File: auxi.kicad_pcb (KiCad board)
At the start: 2 copper layers, 0 parts

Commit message: feat(pcb): Add design settings, update schematic notes, and modify MP1584 module footprint
- Introduced comprehensive design settings in `auxi.kicad_pro` for improved PCB layout control, including defaults for various design elements and DRC rules.
- Updated schematic notes in `auxi.kicad_sch` to reflect changes in battery connector specifications and additional circuit details.
- Enhanced the MP1584 module footprint in `MP1584_Mini_PROVISIONAL.kicad_mod` with corrected dimensions, improved pad layout, and updated silk screen labels for clarity.
- Added a new PCB placement image `auxi_pcb_placement.png` to the documentation for better assembly guidance.
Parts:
- added C1: 470uF 25V, Capacitor_THT:CP_Radial_D10.0mm_P5.00mm, F.Cu at (159.0, 112.0)
- added C10: 100nF 50V X7R, Capacitor_SMD:C_1206_3216Metric, F.Cu at (157.5, 190.5)
- added C11: 470uF 25V, Capacitor_THT:CP_Radial_D10.0mm_P5.00mm, F.Cu at (122.5, 164.0)
- added C12: 10uF 25V X7R, Capacitor_SMD:C_1206_3216Metric, F.Cu at (136.0, 151.0)
- added C13: 100nF 50V X7R, Capacitor_SMD:C_1206_3216Metric, F.Cu at (141.2, 151.0)
- added C14: 10uF 25V X7R, Capacitor_SMD:C_1206_3216Metric, F.Cu at (127.5, 109.5)
- added C15: 100nF 50V X7R, Capacitor_SMD:C_1206_3216Metric, F.Cu at (132.5, 109.5)
- added C16: 10uF 25V X7R, Capacitor_SMD:C_1206_3216Metric, F.Cu at (110.5, 162.0)
- added C17: 100nF 50V X7R, Capacitor_SMD:C_1206_3216Metric, F.Cu at (110.5, 166.0)
- added C18: 10uF 25V X7R, Capacitor_SMD:C_1206_3216Metric, F.Cu at (126.5, 195.0)
- added C19: 100nF 50V X7R, Capacitor_SMD:C_1206_3216Metric, F.Cu at (129.0, 195.0)
- added C2: 100nF 50V X7R, Capacitor_SMD:C_1206_3216Metric, F.Cu at (170.0, 115.0)
- added C20: 10uF 25V X7R, Capacitor_SMD:C_1206_3216Metric, F.Cu at (111.0, 113.0)
- added C21: 100nF 50V X7R, Capacitor_SMD:C_1206_3216Metric, F.Cu at (111.0, 117.0)
- added C3: 220uF 25V, Capacitor_THT:CP_Radial_D8.0mm_P3.50mm, F.Cu at (138.8, 117.5)
- added C4: 100nF 50V X7R, Capacitor_SMD:C_1206_3216Metric, F.Cu at (139.0, 106.5)
- added C5: 22uF 25V, Capacitor_THT:CP_Radial_D5.0mm_P2.00mm, F.Cu at (111.5, 183.0)
- added C6: 100nF 50V X7R, Capacitor_SMD:C_1206_3216Metric, F.Cu at (112.5, 188.0)
- added C7: 100uF 16V, Capacitor_THT:CP_Radial_D6.3mm_P2.50mm, F.Cu at (140.2, 166.0)
- added C8: 10uF 25V X7R, Capacitor_SMD:C_1206_3216Metric, F.Cu at (143.0, 184.0)
- added C9: 100uF 16V, Capacitor_THT:CP_Radial_D6.3mm_P2.50mm, F.Cu at (182.8, 185.0)
- added D1: 1N5819, Diode_THT:D_DO-41_SOD81_P10.16mm_Horizontal, F.Cu at (150.5, 190.0)
- added H1: MountingHole_3.2mm_M3, MountingHole:MountingHole_3.2mm_M3, F.Cu at (105.0, 105.0)
- added H2: MountingHole_3.2mm_M3, MountingHole:MountingHole_3.2mm_M3, F.Cu at (185.0, 105.0)
- added H3: MountingHole_3.2mm_M3, MountingHole:MountingHole_3.2mm_M3, F.Cu at (105.0, 195.0)
- added H4: MountingHole_3.2mm_M3, MountingHole:MountingHole_3.2mm_M3, F.Cu at (185.0, 195.0)
- added J_BAT1: XT30 BAT 2S, Connector_AMASS:AMASS_XT30UPB-M_1x02_P5.0mm_Vertical, F.Cu at (185.5, 120.0)
- added J_LED_FRONT1: LED_FRONT (ROJO), Connector_PinHeader_2.54mm:PinHeader_1x02_P2.54mm_Vertical, F.Cu at (102.5, 176.0)
- added J_LED_LEFT1: LED_LEFT (AMARILLO), Connector_PinHeader_2.54mm:PinHeader_1x02_P2.54mm_Vertical, F.Cu at (132.5, 197.5)
- added J_LED_POWER1: POWER LED (azul), Connector_PinHeader_2.54mm:PinHeader_1x02_P2.54mm_Vertical, F.Cu at (187.5, 128.0)
- added J_LED_RIGHT1: LED_RIGHT (VERDE), Connector_PinHeader_2.54mm:PinHeader_1x02_P2.54mm_Vertical, F.Cu at (110.5, 103.0)
- added J_MOTOR_LEFT1: MOTOR_LEFT, TerminalBlock_Phoenix:TerminalBlock_Phoenix_MKDS-1,5-2-5.08_1x02_P5.08mm_Horizontal, F.Cu at (140.5, 194.5)
- added J_MOTOR_RIGHT1: MOTOR_RIGHT, TerminalBlock_Phoenix:TerminalBlock_Phoenix_MKDS-1,5-2-5.08_1x02_P5.08mm_Horizontal, F.Cu at (151.0, 107.0)
- added J_SENSOR_FRONT1: SENSOR_FRONT (VL53L0X), Connector_JST:JST_XH_B5B-XH-A_1x05_P2.50mm_Vertical, F.Cu at (104.5, 161.0)
- added J_SENSOR_LEFT1: SENSOR_LEFT (VL53L0X), Connector_JST:JST_XH_B5B-XH-A_1x05_P2.50mm_Vertical, F.Cu at (122.0, 196.5)
- added J_SENSOR_RIGHT1: SENSOR_RIGHT (VL53L0X), Connector_JST:JST_XH_B5B-XH-A_1x05_P2.50mm_Vertical, F.Cu at (104.5, 112.0)
- added J_SWITCH1: SWITCH ON-OFF, TerminalBlock_Phoenix:TerminalBlock_Phoenix_MKDS-1,5-2-5.08_1x02_P5.08mm_Horizontal, F.Cu at (175.0, 106.0)
- added R1: 1.5k, Resistor_SMD:R_1206_3216Metric, F.Cu at (183.0, 129.3)
- added R2: 10k, Resistor_SMD:R_1206_3216Metric, F.Cu at (127.5, 118.5)
- added R3: 4.7k DNP, Resistor_SMD:R_1206_3216Metric, F.Cu at (160.0, 167.6)
- added R4: 4.7k DNP, Resistor_SMD:R_1206_3216Metric, F.Cu at (160.0, 175.2)
- added R5: 470, Resistor_SMD:R_1206_3216Metric, F.Cu at (108.0, 177.0)
- added R6: 470, Resistor_SMD:R_1206_3216Metric, F.Cu at (135.0, 192.5)
- added R7: 470, Resistor_SMD:R_1206_3216Metric, F.Cu at (111.5, 108.3)
- added U_CAM1: ESP32-CAM AI Thinker (fila 5V), Connector_PinSocket_2.54mm:PinSocket_1x08_P2.54mm_Vertical, F.Cu at (142.5, 154.9)
- added U_CAM2: ESP32-CAM AI Thinker (fila 3V3), Connector_PinSocket_2.54mm:PinSocket_1x08_P2.54mm_Vertical, F.Cu at (142.5, 132.1)
- added U_ESP_J1: ESP32-S3-DevKitC-1 N16R8 (J1), Connector_PinSocket_2.54mm:PinSocket_1x22_P2.54mm_Vertical, F.Cu at (154.0, 139.7)
- added U_ESP_J3: ESP32-S3-DevKitC-1 N16R8 (J3), Connector_PinSocket_2.54mm:PinSocket_1x22_P2.54mm_Vertical, F.Cu at (176.9, 139.7)
- added U_MP1584: MP1584EN mini (5.0V), auxi:MP1584_Mini_PROVISIONAL, F.Cu at (129.2, 179.5)
- added U_TB1: TB6612FNG breakout (logica), Connector_PinSocket_2.54mm:PinSocket_1x08_P2.54mm_Vertical, F.Cu at (134.9, 122.9)
- added U_TB2: TB6612FNG breakout (potencia), Connector_PinSocket_2.54mm:PinSocket_1x08_P2.54mm_Vertical, F.Cu at (134.9, 105.1)
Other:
- board outline added: 90 x 100 mm
- board text added: "5V"
- board text added: "ANT/FPC"
- board text added: "ANTENNA - NO COPPER"
- board text added: "ESP32-CAM"
- board text added: "ESP32-S3-DevKitC-1"
- board text added: "TB6612FNG"
- board text added: "USB"
- board text added: "VM"

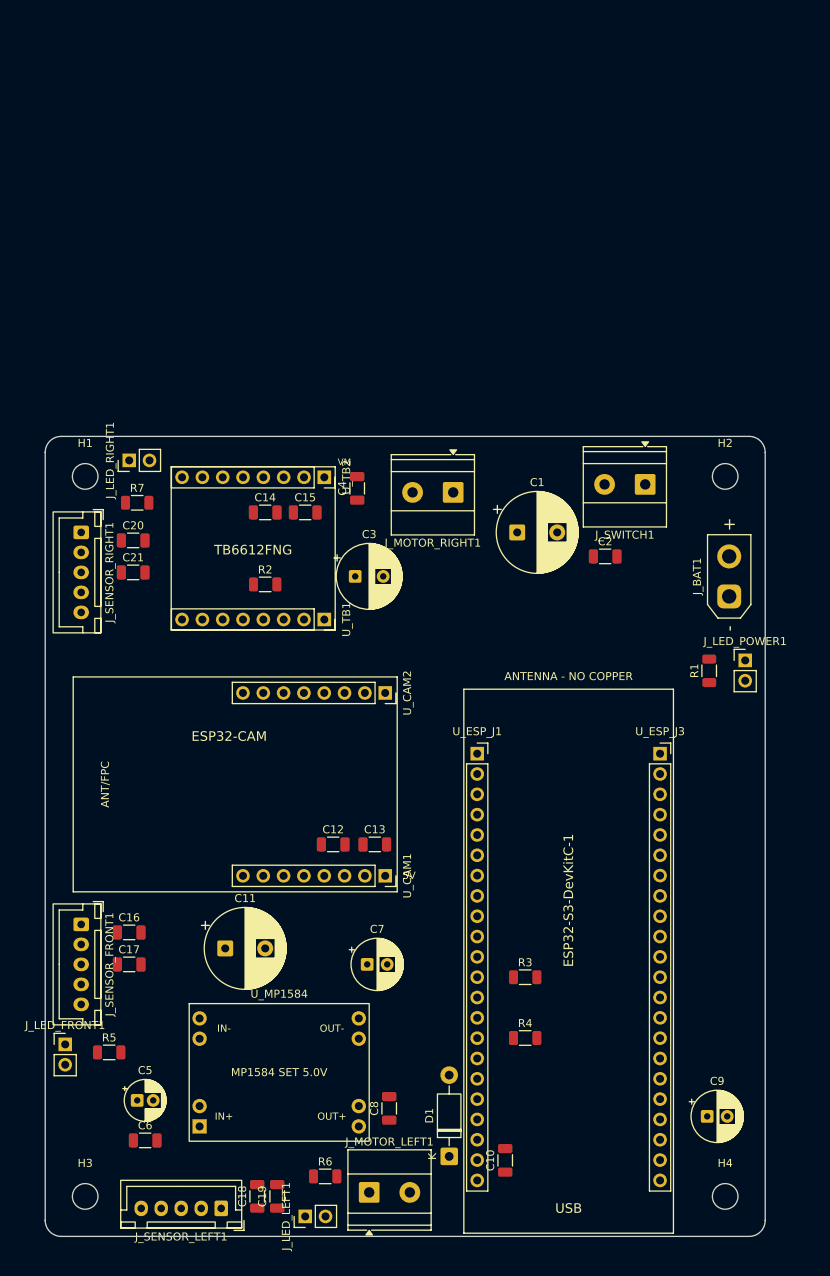
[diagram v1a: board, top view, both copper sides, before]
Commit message: Add initial DRC violations report, update BOM with correct footprints, modify schematic for clarity, and add PCB top image
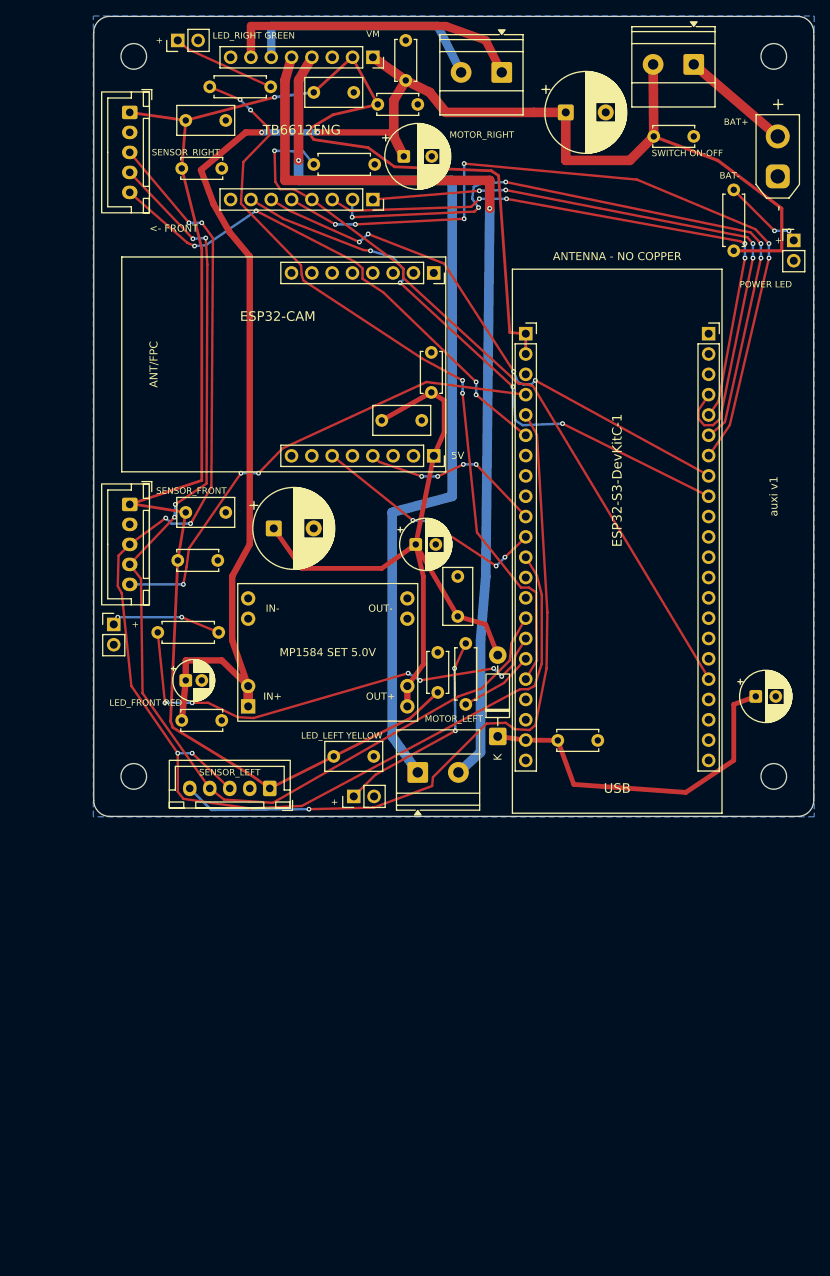
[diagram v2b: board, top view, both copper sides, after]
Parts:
- removed R6, R7: 470, Resistor_SMD:R_1206_3216Metric
- C10, C13, C15, C17, C19, C2, C21, C4, C6: footprint Capacitor_SMD:C_1206_3216Metric -> Capacitor_THT:C_Disc_D5.0mm_W2.5mm_P5.00mm
- C12, C14, C16, C18, C20, C8: footprint Capacitor_SMD:C_1206_3216Metric -> Capacitor_THT:C_Rect_L7.0mm_W3.5mm_P5.00mm
- R1, R2, R5: footprint Resistor_SMD:R_1206_3216Metric -> Resistor_THT:R_Axial_DIN0207_L6.3mm_D2.5mm_P7.62mm_Horizontal
- R3, R4: value 4.7k DNP -> 470; footprint Resistor_SMD:R_1206_3216Metric -> Resistor_THT:R_Axial_DIN0207_L6.3mm_D2.5mm_P7.62mm_Horizontal
- moved R5 121.4 mm to (120.6, 56.3)
- moved C19 66.1 mm to (149.1, 132.0)
- moved R3 63.0 mm to (114.1, 124.5)
- moved C8 62.1 mm to (151.6, 122.5)
- moved C13 56.9 mm to (148.3, 94.5), turned to 90 degrees
- moved C18 55.8 mm to (136.1, 140.0), turned to 0 degrees
- moved C12 53.3 mm to (142.1, 98.0)
- moved C16 53.0 mm to (117.6, 109.5)
- moved C10 52.9 mm to (164.1, 138.0), turned to 0 degrees
- moved C20 52.9 mm to (117.6, 60.5)
- moved U_TB1 52.8 mm to (141.0, 70.4)
- moved U_TB2 52.8 mm to (141.0, 52.6)
- moved C1 52.8 mm to (165.1, 59.5)
- moved C11 52.8 mm to (128.6, 111.5)
- moved C14 52.8 mm to (133.6, 57.0)
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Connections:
- R3 pad 1: +3V3 -> LED_FRONT
- R3 pad 2: SDA -> LED_FRONT_A
- R4 pad 1: +3V3 -> LED_LEFT
- R4 pad 2: SCL -> LED_LEFT_A
- R5 pad 1: LED_FRONT -> LED_RIGHT
- R5 pad 2: LED_FRONT_A -> LED_RIGHT_A
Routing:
- net +3V3: track 0.00 -> 222.5 mm, vias 0 -> 1
- net +VBAT_SW: track 0.00 -> 209.0 mm, vias 0 -> 2
- net SDA: track 0.00 -> 168.1 mm, vias 0 -> 6
- net SCL: track 0.00 -> 138.3 mm, vias 0 -> 4
- net M_L2: track 0.00 -> 116.4 mm, vias 0 -> 1
- net M_L1: track 0.00 -> 115.8 mm, vias 0 -> 1
- net BIN1: track 0.00 -> 97.4 mm, vias 0 -> 6
- net LED_RIGHT: track 0.00 -> 97.3 mm, vias 0 -> 4
- net STBY: track 0.00 -> 94.5 mm, vias 0 -> 1
- net XSHUT_LEFT: track 0.00 -> 88.4 mm, vias 0 -> 1
- net +5V: track 0.00 -> 88.0 mm
- net AIN2: track 0.00 -> 83.7 mm, vias 0 -> 5
- net PWMA: track 0.00 -> 77.6 mm, vias 0 -> 4
- net AIN1: track 0.00 -> 75.0 mm, vias 0 -> 4
- net PWMB: track 0.00 -> 73.0 mm, vias 0 -> 4
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- added copper zone on B.Cu, net GND
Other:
- board text added: "+"
- board text added: "<- FRONT"
- board text added: "BAT+"
- board text added: "BAT-"
- board text added: "LED_FRONT RED"
- board text added: "LED_LEFT YELLOW"
- board text added: "LED_RIGHT GREEN"
- board text added: "MOTOR_LEFT"
- board text added: "MOTOR_RIGHT"
- board text added: "POWER LED"
- board text added: "SENSOR_FRONT"
- board text added: "SENSOR_LEFT"
- board text added: "SENSOR_RIGHT"
- board text added: "SWITCH ON-OFF"
- board text added: "auxi v1"

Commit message: Refactor schematic and DRC violation files
- Removed unnecessary wire segments from auxi.kicad_sch to clean up the schematic.
- Added new wire connections to enhance circuit clarity in auxi.kicad_sch.
- Updated timestamp in auxi_drc_violations.json to reflect the latest changes.
- Added a new PDF document (auxi_pcb_real_scale.pdf) containing detailed PCB layouts for both top and bottom layers.
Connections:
- J_MOTOR_RIGHT1 pad 1: M_R1 -> M_R2
- J_MOTOR_RIGHT1 pad 2: M_R2 -> M_R1
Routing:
- net M_R2: track 31.2 -> 34.6 mm
- net M_R1: track 38.0 -> 38.6 mm
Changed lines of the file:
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@@
 		(legacy_teardrops no)
 	)
-	(paper "A4")
+	(paper "A" portrait)
 	(title_block
 		(title "auxi")
@@
 			(remove_unused_layers no)
 			(roundrect_rratio 0.096154)
-			(net "M_R1")
+			(net "M_R2")
 		)
 		(pad "2" thru_hole circle
@@
 			(layers "*.Cu" "*.Mask")
 			(remove_unused_layers no)
-			(net "M_R2")
+			(net "M_R1")
 		)
 		(embedded_fonts no)
@@
 	)
 	(segment
+		(start 128.26 48.7)
+		(end 149.07 48.7)
+		(width 1.05)
+		(layer "B.Cu")
+		(net "M_R2")
+	)
+	(segment
+		(start 149.07 48.7)
+		(end 157.07 54.5)
+		(width 1.05)
+		(layer "B.Cu")
+		(net "M_R2")
+	)
+	(segment
+		(start 128.26 52.61)
+		(end 128.26 48.7)
+		(width 1.05)
+		(layer "B.Cu")
+		(net "M_R2")
+	)
+	(segment
 		(start 125.72 52.61)
 		(end 125.72 48.7)
@@
 	(segment
 		(start 155.07 50.5)
-		(end 157.07 54.5)
+		(end 151.99 54.5)
 		(width 1.05)
 		(layer "F.Cu")
@@
 	)
 	(segment
-		(start 128.26 48.7)
-		(end 149.07 48.7)
-		(width 1.05)
-		(layer "B.Cu")
-		(net "M_R2")
-	)
-	(segment
-		(start 149.07 48.7)
-		(end 151.99 54.5)
-		(width 1.05)
-		(layer "B.Cu")
-		(net "M_R2")
-	)
-	(segment
-		(start 128.26 52.61)
-		(end 128.26 48.7)
-		(width 1.05)
-		(layer "B.Cu")
-		(net "M_R2")
-	)
-	(segment
